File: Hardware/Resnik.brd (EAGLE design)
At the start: 64.8 x 100 mm, 180 parts, among them IC1 ATMEGA644M, J1 CONN_82.54_SCREW, J3 CONN_42.54_SCREW, J4 CONN_82.54_SCREW, Q1 DMG3404, Q2 DMG3404, Q3 FDN360P, Q4 FDN360P, Q5 FDN360P, Q6 DMG3404, U1 TLV61220DBV, U10 TPS22917DBV, U11 SN74AUP1G04YFP, U12 SN74AUP1G04YFP, U13 SN74AUP2G86SOT833-1, U14 SN74AUP2G08DQE, U15 SN74AUP2G08DQE, U16 SN74AUP2G08DQE, U17 MIC2039MT, U18 MIC2039MT, U19 MIC2039MT, U2 TPS62822DLC, U20 MIC2039MT, U21 TPS22917DBV, U22 TPS22917DBV, U23 FT231X-Q, U24 SN74LVC1G3157DRL, U25 SN74AUP3G34DCU, U26 TXS0102DQM, U27 TXS0108RGY, U28 TXS0108RGY, U29 TXS0104RGY, U3 TPS61032RSA, U30 MCP4726A2SOT-23, U31 BME280, U32 ADS1115, U33 ADS1115, U34 INA211DCK, U35 INA210DCK, U36 TCA9555RTW, U5 BQ2980RUG, U6 TPS2105, U7 LTC4412S6, U8 TPL5111DDC, U9 TPS79733

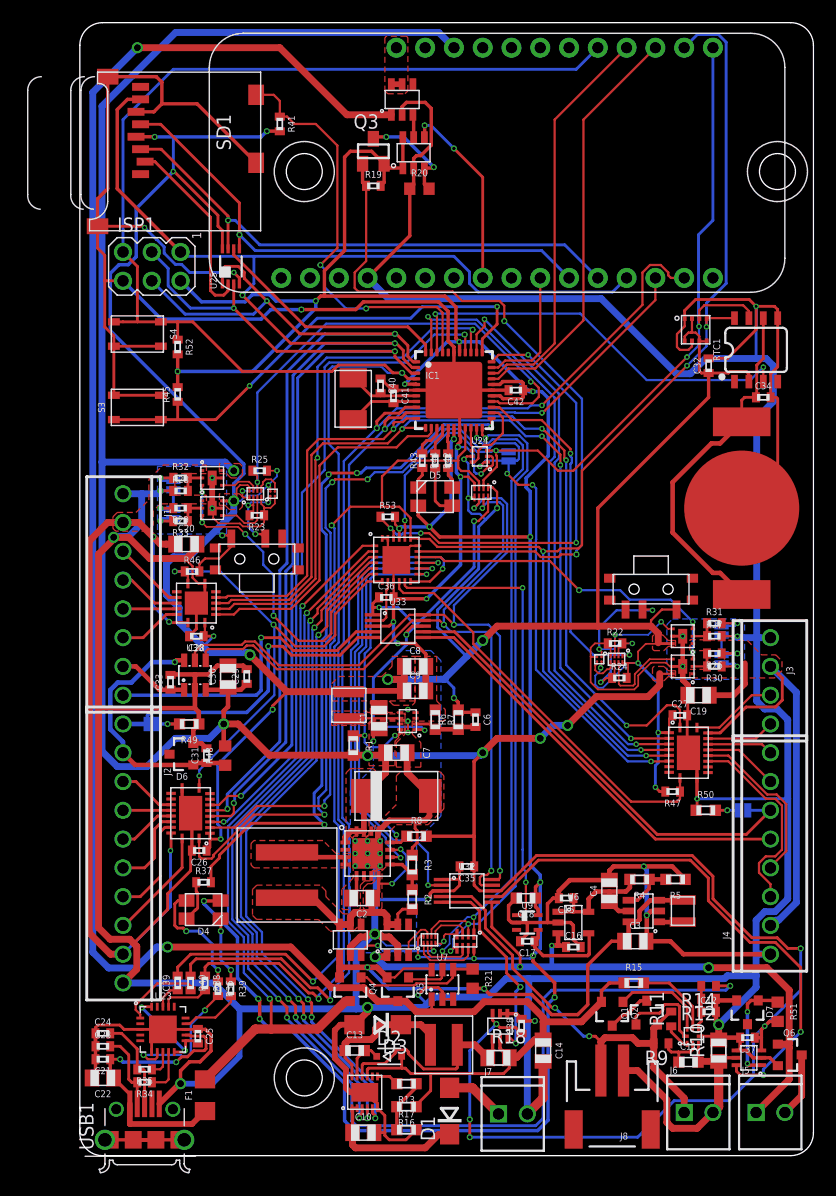
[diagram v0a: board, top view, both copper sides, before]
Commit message: Updated BOM info
Added info to schematic to support auto-generating BOM
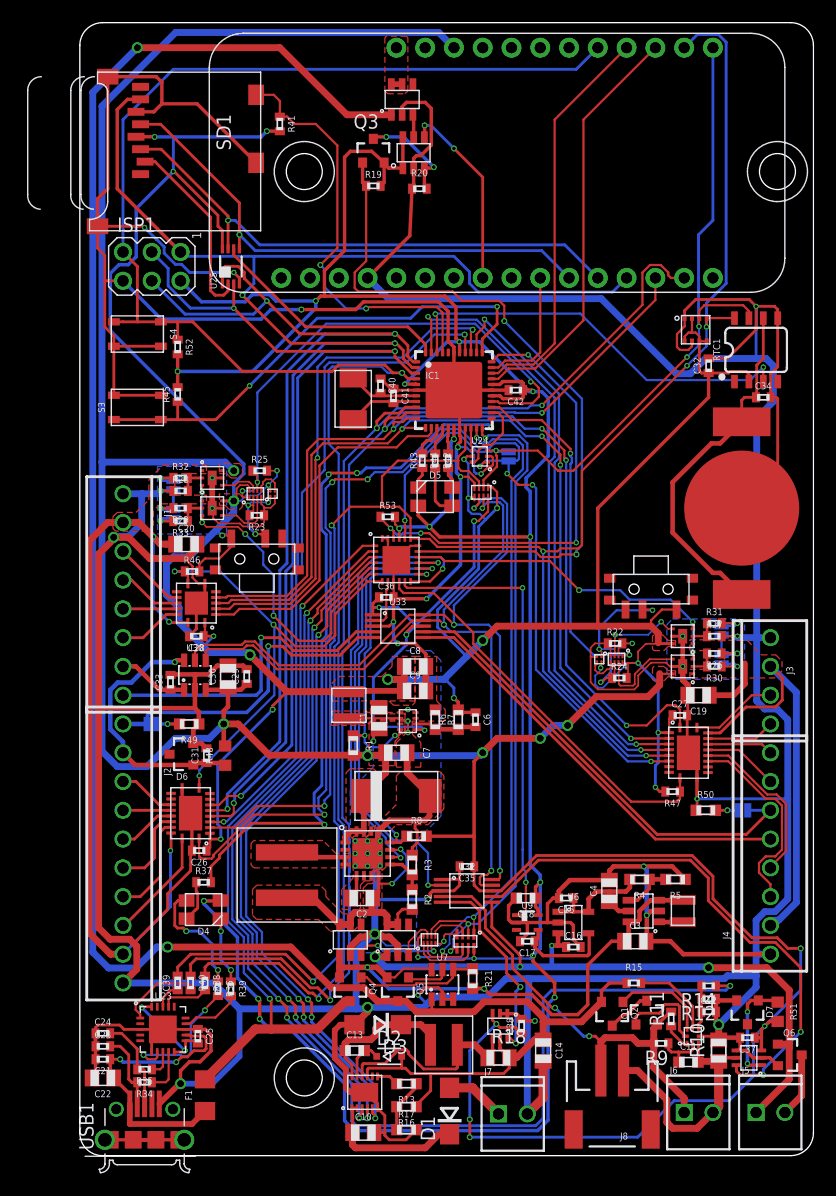
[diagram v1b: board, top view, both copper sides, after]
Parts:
- C26, C27, C28, C34: value (none) -> 0.1uF
- C7: value 2.2uF -> 22uF
- Q3: device transistor-power:SUPER-SOT3 -> bschulz:SOT23-3
- R11: value 20R -> 20; device bschulz:R0402 -> bschulz_passives:R0402
- R12, R14: device bschulz:R0402 -> bschulz_passives:R0402
- R15: device bschulz_passives:R0603 -> bschulz_passives:R0402
- R19: value 180k -> 120k
- R20: device bschulz:R0603 -> bschulz_passives:R0402
- R21: value (none) -> 470k; device bschulz:R0603 -> bschulz_passives:R0603
- R9: value 330R -> 330; device bschulz:R0402 -> bschulz_passives:R0402

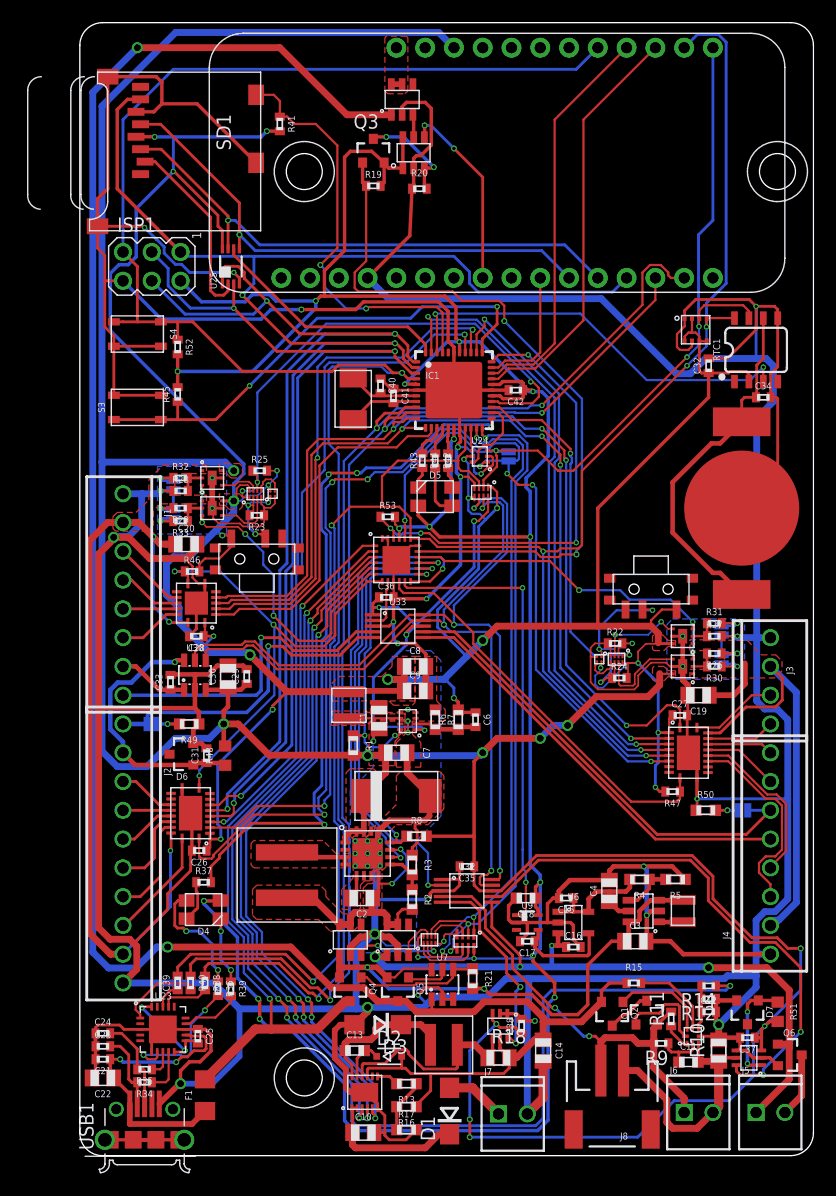
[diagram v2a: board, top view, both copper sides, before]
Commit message: First round of fixes to hardware
changed SD card holder, power switches, power switch topology, add pull up resistors to IO expander, to allow for new non-internal pull up module, added some silkscreen, added 3v3 core I2C pullups
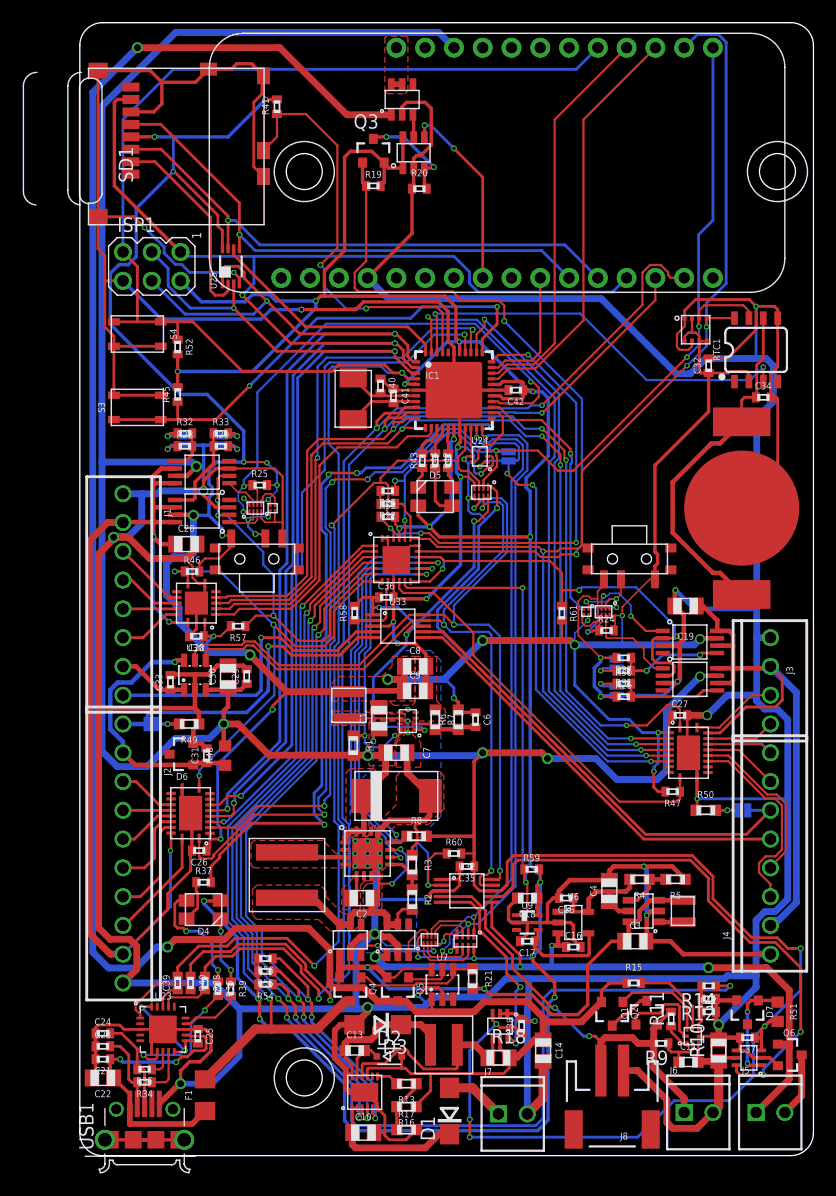
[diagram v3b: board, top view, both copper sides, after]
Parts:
- added R54, R55, R56, R57, R58, R59, R60, R61: (no value), bschulz_passives:R0402
- R22, R23: value 10k -> (none)
- SD1: value MICROSD -> MICROSDCD; device bschulz:MICROSD -> bschulz:MICROSD_CD
- U17, U18, U19, U20: value MIC2039MT -> MIC2544MSOP; device bschulz:DFN_6_2X2 -> bschulz:MSOP_8
- moved R22 23.5 mm to (27.2, 57.5), turned to 180 degrees
- moved SD1 20.3 mm to (0.76, 82.2), turned to 90 degrees
- moved R23 11.8 mm to (27.2, 58.7)
- moved JP2 9.72 mm to (47.4, 43.4), turned to 270 degrees
- moved JP1 9.68 mm to (47.4, 41.0), turned to 90 degrees
- moved R31 9.03 mm to (48.0, 42.8), turned to 180 degrees
- moved R26 8.86 mm to (48.0, 40.5), turned to 0 degrees
- moved R33 8.52 mm to (12.4, 63.8), turned to 0 degrees
- moved R27 8.22 mm to (48.0, 43.9), turned to 180 degrees
- moved R30 8.14 mm to (48.0, 41.7), turned to 0 degrees
- moved C19 7.96 mm to (53.5, 48.5)
- moved JP4 7.71 mm to (12.4, 63.1), turned to 90 degrees
- moved R29 6.52 mm to (12.4, 62.6), turned to 0 degrees
- moved U11 4.34 mm to (44.7, 48.0)
- moved U14 4.34 mm to (46.2, 48.0)
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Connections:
- net 3V3_AUX: now also R57.2, R61.2, U18.7, U20.7; no longer U18.6, U20.6
- net 3V3_CORE: now also R22.2, R23.2, R54.2, R55.2, R56.2, R59.2
- net 5V_AUX: now also R58.2, R60.2, U17.7, U19.7; no longer U17.6, U19.6
- net ADC_EXT_ALERT: now also R58.1
- net ADC_OB_ALERT: now also R60.1
- net FAULT_PRIME: now also R57.1, U19.2, U20.2; no longer U19.3, U20.3
- net FAULT_SEC: now also R61.1, U17.2, U18.2; no longer U17.3, U18.3
- net GND: now also S1.3, S2.3, SD1.MT3, SD1.MT4, U17.3, U18.3, U19.3, U20.3; no longer R22.1, R23.1, U17.5, U17.PAD, U17.PAD@1, U18.5, U18.PAD, U18.PAD@1, U19.5, U19.PAD, U19.PAD@1, U20.5, U20.PAD, U20.PAD@1
- net MPPT_CHRG: now also R55.1
- net MPPT_FAULT: now also R56.1
- net MPPT_SHDN: now also R54.1
- net N$27: now also U19.5; no longer U19.2
- net N$28: no longer R23.2
- net N$29: now also U19.1; no longer U19.4
- net N$30: now also U20.1; no longer U20.4
- net N$33: now also U20.5; no longer U20.2
- net N$35: no longer R22.2
- net N$36: now also U17.1; no longer U17.4
- net N$37: now also U18.1; no longer U18.4
- net N$38: now also U17.5; no longer U17.2
- net N$41: now also U18.5; no longer U18.2
- net PG_LDO: now also R59.1
- net SCL: now also R22.1
- net SDA_OB: now also R23.1
- net VBUS_PRIME: now also U19.6, U19.8, U20.6, U20.8; no longer U19.1, U20.1
- net VBUS_SEC: now also U17.6, U17.8, U18.6, U18.8; no longer U17.1, U18.1
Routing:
- net GND: track 798.1 -> 845.0 mm, vias 29 -> 33
- net 5V_AUX: track 333.1 -> 344.8 mm
- net 3V3_AUX: track 271.1 -> 282.7 mm, vias 21 -> 26
- net VBUS_PRIME: track 71.1 -> 82.5 mm
- net VBUS_SEC: track 41.4 -> 52.7 mm
- net 3V3_CORE: track 252.3 -> 260.3 mm
- net N$35: track 14.1 -> 6.99 mm, vias 3 -> 2
- net N$41: track 2.39 -> 9.38 mm, vias 0 -> 2
- net N$38: track 2.39 -> 8.96 mm
- net FAULT_SEC: track 30.5 -> 36.5 mm, vias 3 -> 2
- net N$33: track 2.39 -> 8.23 mm
- net MPPT_FAULT: track 59.2 -> 64.7 mm
- net EN_BUS_SEC: track 36.8 -> 31.7 mm
- net ADC_OB_ALERT: track 41.6 -> 45.6 mm
- net MPPT_CHRG: track 59.7 -> 63.7 mm
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- removed copper zone on layer 1, net VBUS_PRIME
- removed copper zone on layer 1, net VBUS_SEC
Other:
- board text added: "AUX"
- board text added: "LOG"
- board text added: "RST"
- board text added: "STAT"

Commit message: Layout fixes
Improvements and cleanup in the layout, should get final review before being sent out to fab
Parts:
- moved U11 1.40 mm to (46.1, 47.9)
- moved U14 1.40 mm to (47.6, 47.9)
- moved R24 1.40 mm to (47.9, 46.2)
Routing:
- net N$37: track 8.37 -> 6.92 mm
- net N$36: track 8.50 -> 7.05 mm
- net EN_BUS_SEC: track 31.7 -> 32.5 mm
- net FAULT_SEC: track 36.5 -> 37.2 mm
- net 3V3_AUX: track 282.7 -> 282.1 mm

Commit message: Generated Gerbers, Minor Updates
v0.1 Sent to fab
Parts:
- moved U$4 5.08 mm to (20.2, 64.5)
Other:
- board text added: "Project Resnik v0.1 ---------------- Developed by Northern Widget and University of Minnesota"
- board text removed: "Project Resnik v0.0 ---------------- Developed by Northern Widget and University of Minnesota"
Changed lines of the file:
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@@
 <?xml version="1.0" encoding="utf-8"?>
 <!DOCTYPE eagle SYSTEM "eagle.dtd">
-<eagle version="9.2.1">
+<eagle version="9.2.2">
 <drawing>
 <settings>
@@
 <layer number="20" name="Dimension" color="24" fill="1" visible="yes" active="yes"/>
 <layer number="21" name="tPlace" color="7" fill="1" visible="yes" active="yes"/>
-<layer number="22" name="bPlace" color="7" fill="1" visible="no" active="yes"/>
+<layer number="22" name="bPlace" color="7" fill="1" visible="yes" active="yes"/>
 <layer number="23" name="tOrigins" color="15" fill="1" visible="yes" active="yes"/>
 <layer number="24" name="bOrigins" color="15" fill="1" visible="yes" active="yes"/>
@@
 <layer number="50" name="dxf" color="7" fill="1" visible="no" active="no"/>
 <layer number="51" name="tDocu" color="7" fill="1" visible="yes" active="yes"/>
-<layer number="52" name="bDocu" color="7" fill="1" visible="no" active="yes"/>
+<layer number="52" name="bDocu" color="7" fill="1" visible="yes" active="yes"/>
 <layer number="53" name="tGND_GNDA" color="7" fill="1" visible="no" active="no"/>
 <layer number="54" name="bGND_GNDA" color="7" fill="1" visible="no" active="no"/>
@@
 <wire x1="62.75" y1="100" x2="2" y2="100" width="0" layer="20"/>
 <wire x1="2" y1="100" x2="0" y2="98" width="0" layer="20" curve="90"/>
-<text x="52.959" y="52.451" size="0.8128" layer="51" font="vector" ratio="15" align="center">5v</text>
-<text x="47.752" y="52.451" size="0.8128" layer="51" font="vector" ratio="15" align="center">3v3</text>
+<text x="50.927" y="54.864" size="0.8128" layer="51" font="vector" ratio="15" align="center">5v</text>
+<text x="45.72" y="54.864" size="0.8128" layer="51" font="vector" ratio="15" align="center">3v3</text>
 <text x="18.288" y="50.165" size="0.8128" layer="51" font="vector" ratio="15" align="center">3v3</text>
 <text x="13.208" y="50.165" size="0.8128" layer="51" font="vector" ratio="15" align="center">5v</text>
@@
 <text x="6.35" y="46.99" size="1.27" layer="52" font="vector" ratio="15" rot="MR270" align="center">Primary Bus</text>
 <text x="58.801" y="21.59" size="1.27" layer="52" font="vector" ratio="15" rot="MR270" align="center">Secondary Bus</text>
-<text x="62.23" y="62.23" size="1.27" layer="52" font="vector" ratio="15" rot="MR0" align="center-left">Project Resnik v0.0
+<text x="62.23" y="62.23" size="1.27" layer="52" font="vector" ratio="15" rot="MR0" align="center-left">Project Resnik v0.1
 ----------------
 Developed by
@@
 <attribute name="VALUE_PART" value="10k" x="27.178" y="56.388" size="1.778" layer="27" display="off"/>
 </element>
-<element name="U$4" library="awickert" package="NWLOGO_MED" value="" x="15.113" y="64.516" smashed="yes" rot="MR0"/>
+<element name="U$4" library="awickert" package="NWLOGO_MED" value="" x="20.193" y="64.516" smashed="yes" rot="MR0"/>
 <element name="R54" library="bschulz_passives" package="R0402" value="" x="16.383" y="15.113" smashed="yes" rot="R180">
 <attribute name="DIGIKEY" value="" x="16.383" y="15.113" size="0.6096" layer="27" font="vector" ratio="15" rot="R180" display="off"/>
@@
 <wire x1="10.287" y1="60.833" x2="9.454" y2="60" width="0.4064" layer="1"/>
 <wire x1="9.454" y1="60" x2="8.395" y2="60" width="0.4064" layer="1"/>
-<via x="54.737" y="42.291" extent="1-16" drill="0.6"/>
+<via x="54.737" y="42.291" extent="1-16" drill="0.6" diameter="1"/>
 <wire x1="51.7652" y1="39.3192" x2="54.737" y2="42.291" width="0.6096" layer="16"/>
 <wire x1="45.54434375" y1="35.052" x2="47.39854375" y2="33.1978" width="0.6096" layer="16"/>
@@
 <contactref element="SD1" pad="MT4"/>
 <wire x1="7.112" y1="58.674" x2="10.922" y2="58.674" width="0.6096" layer="16"/>
-<via x="10.922" y="58.674" extent="1-16" drill="0.6"/>
+<via x="10.922" y="58.674" extent="1-16" drill="0.6" diameter="1"/>
 <wire x1="10.922" y1="58.674" x2="10.922" y2="59.563" width="0.3048" layer="1"/>
 <wire x1="12.009" y1="60.65" x2="13.195" y2="60.65" width="0.3048" layer="1"/>
@@
 <wire x1="59.7408" y1="40.64" x2="57.15" y2="40.64" width="0.6096" layer="16"/>
 <wire x1="57.15" y1="40.64" x2="55.372" y2="38.862" width="0.6096" layer="16"/>
-<via x="55.372" y="38.862" extent="1-16" drill="0.6"/>
+<via x="55.372" y="38.862" extent="1-16" drill="0.6" diameter="1"/>
 <wire x1="55.372" y1="38.862" x2="53.609" y2="38.862" width="0.6096" layer="1"/>
 <wire x1="52.959" y1="44.958" x2="52.959" y2="42.037" width="0.4064" layer="1"/>
@@
 <wire x1="8.89" y1="67.183" x2="2.6924" y2="73.3806" width="0.3048" layer="16"/>
 <wire x1="2.6924" y1="73.3806" x2="2.6924" y2="77.8764" width="0.3048" layer="16"/>
-<wire x1="11.02073125" y1="56.515" x2="11.02073125" y2="57.70528125" width="0.3048" layer="16"/>
-<wire x1="11.02073125" y1="57.70528125" x2="11.6768" y2="58.36135" width="0.3048" layer="16"/>
-<wire x1="11.6768" y1="58.36135" x2="11.6768" y2="58.98665" width="0.3048" layer="16"/>
-<wire x1="11.6768" y1="58.98665" x2="11.40173125" y2="59.26171875" width="0.3048" layer="16"/>
-<wire x1="11.40173125" y1="59.26171875" x2="11.40173125" y2="59.91573125" width="0.3048" layer="16"/>
+<wire x1="11.02073125" y1="56.515" x2="11.02073125" y2="57.57828125" width="0.3048" layer="16"/>
+<wire x1="11.02073125" y1="57.57828125" x2="11.8038" y2="58.36135" width="0.3048" layer="16"/>
+<wire x1="11.8038" y1="58.36135" x2="11.8038" y2="58.98665" width="0.3048" layer="16"/>
+<wire x1="11.8038" y1="58.98665" x2="11.40173125" y2="59.38871875" width="0.3048" layer="16"/>
+<wire x1="11.40173125" y1="59.38871875" x2="11.40173125" y2="59.91573125" width="0.3048" layer="16"/>
 <wire x1="12.7" y1="61.214" x2="14.4708" y2="61.214" width="0.3048" layer="16"/>
 <wire x1="11.40173125" y1="59.91573125" x2="12.7" y2="61.214" width="0.3048" layer="16"/>
@@
 <wire x1="42.418" y1="45.466" x2="43.307" y2="45.466" width="0.6096" layer="1"/>
 <wire x1="43.307" y1="45.466" x2="43.688" y2="45.085" width="0.6096" layer="1"/>
-<via x="43.688" y="45.085" extent="1-16" drill="0.6"/>
+<via x="43.688" y="45.085" extent="1-16" drill="0.6" diameter="1"/>
 <wire x1="43.688" y1="45.085" x2="49.27194375" y2="45.085" width="0.6096" layer="16"/>
 <wire x1="49.27194375" y1="45.085" x2="54.229" y2="45.085" width="0.6096" layer="16"/>
 <wire x1="54.229" y1="45.085" x2="54.737" y2="45.593" width="0.6096" layer="16"/>
-<via x="54.737" y="45.593" extent="1-16" drill="0.6"/>
+<via x="54.737" y="45.593" extent="1-16" drill="0.6" diameter="1"/>
 <wire x1="46.228" y1="47.117" x2="44.196" y2="45.085" width="0.1524" layer="16"/>
 <wire x1="43.688" y1="45.085" x2="44.196" y2="45.085" width="0.1524" layer="16"/>
@@
 <wire x1="11.796" y1="62.611" x2="11.796" y2="63.754" width="0.254" layer="1"/>
 <wire x1="11.796" y1="62.611" x2="11.796" y2="61.08358125" width="0.3048" layer="1"/>
-<wire x1="11.796" y1="61.08358125" x2="10.1672" y2="59.45478125" width="0.3048" layer="1"/>
-<wire x1="10.1672" y1="59.45478125" x2="10.1672" y2="58.0462" width="0.3048" layer="1"/>
-<wire x1="9.992" y1="57.871" x2="8.395" y2="57.871" width="0.3048" layer="1"/>
-<wire x1="10.1672" y1="58.0462" x2="9.992" y2="57.871" width="0.3048" layer="1"/>
+<wire x1="11.796" y1="61.08358125" x2="10.0402" y2="59.32778125" width="0.3048" layer="1"/>
+<wire x1="10.0402" y1="59.32778125" x2="10.0402" y2="58.3002" width="0.3048" layer="1"/>
+<wire x1="9.611" y1="57.871" x2="8.395" y2="57.871" width="0.3048" layer="1"/>
+<wire x1="10.0402" y1="58.3002" x2="9.611" y2="57.871" width="0.3048" layer="1"/>
 </signal>
 <signal name="VBUS_PRIME">
